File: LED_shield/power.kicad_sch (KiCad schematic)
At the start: 70 parts, among them J301 Screw_Terminal_01x02, Q301 NMOS, Q302 NMOS, Q303 NMOS, Q304 NMOS, Q305 NMOS, U301 LM25149RGYR, U302 LM25149RGYR, U303 LM74700

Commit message: Finish most of PCB design
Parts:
- removed R310, R311: 5m, Resistor_SMD:R_2010_5025Metric, symbol Device:R_US
- added NT301: NetTie_2, NetTie:NetTie-2_SMD_Pad2.0mm, symbol Device:NetTie_2
- C310: renamed from C303; LCSC (none) -> C15195
- C311: renamed from C318; LCSC (none) -> C15195
- C314: renamed from C304; LCSC (none) -> C15195
- C315: renamed from C319; LCSC (none) -> C15195
- C318: renamed from C305; LCSC (none) -> C15195
- C319: renamed from C320; LCSC (none) -> C15195
- C320: renamed from C306; LCSC (none) -> C15195
- C321: LCSC (none) -> C15195
- C322: renamed from C333; LCSC (none) -> C15195
- C323: renamed from C334; LCSC (none) -> C15195
- renumbered C335 to C301, C337 to C302, C336 to C303, C309 to C304, C301 to C305, C316 to C306, C324 to C307, C302 to C308, C317 to C309, C315 to C312, C330 to C313, C314 to C316, C329 to C317, C307 to C324, C322 to C325, C308 to C326, C323 to C327, C310 to C328, C325 to C329, C311 to C330, C326 to C331, C312 to C332, C327 to C333, C313 to C334, C328 to C335, C331 to C336, C332 to C337, R318 to R301, R305 to R302, R306 to R303, R316 to R304, R317 to R305, R307 to R306, R319 to R307, R303 to R308, R314 to R309, R308 to R310, R320 to R311, R309 to R313, R321 to R314, R323 to R315, R324 to R316, R313 to R317, R322 to R318, R304 to R319, R315 to R320, U303 to U301, U301 to U302, U302 to U303
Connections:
- net +5V: now also NT301.2
- net +5V_{b}: now also NT301.1
- no-connect marks 5 -> 7

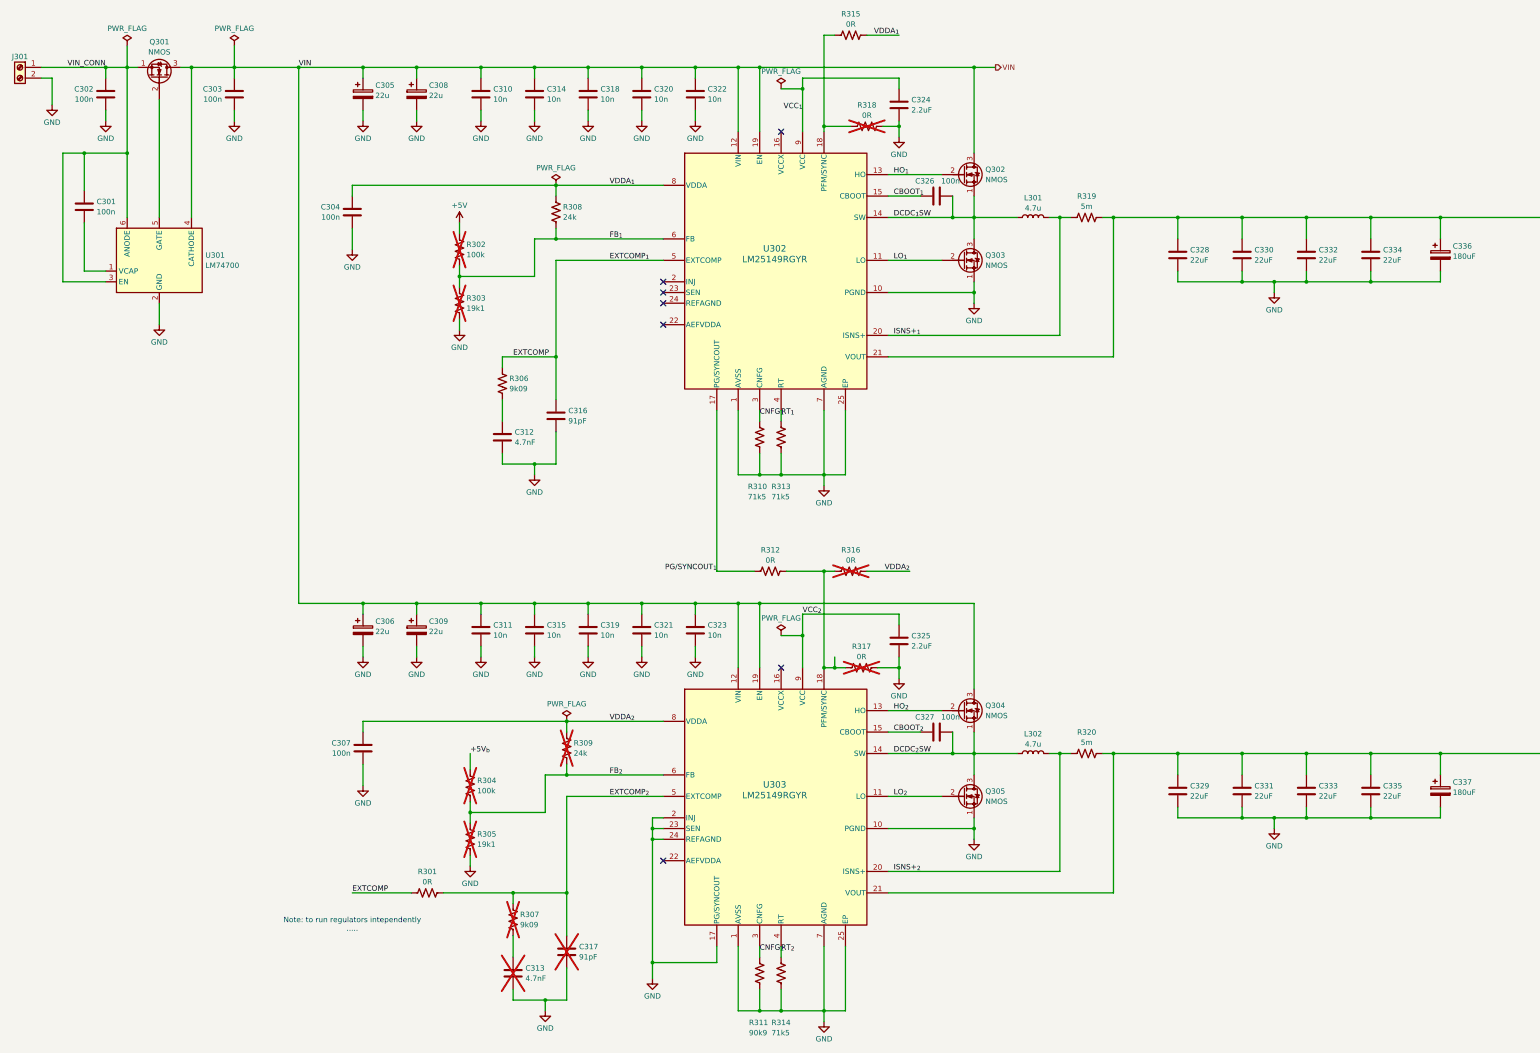
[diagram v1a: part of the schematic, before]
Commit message: Remove unused components
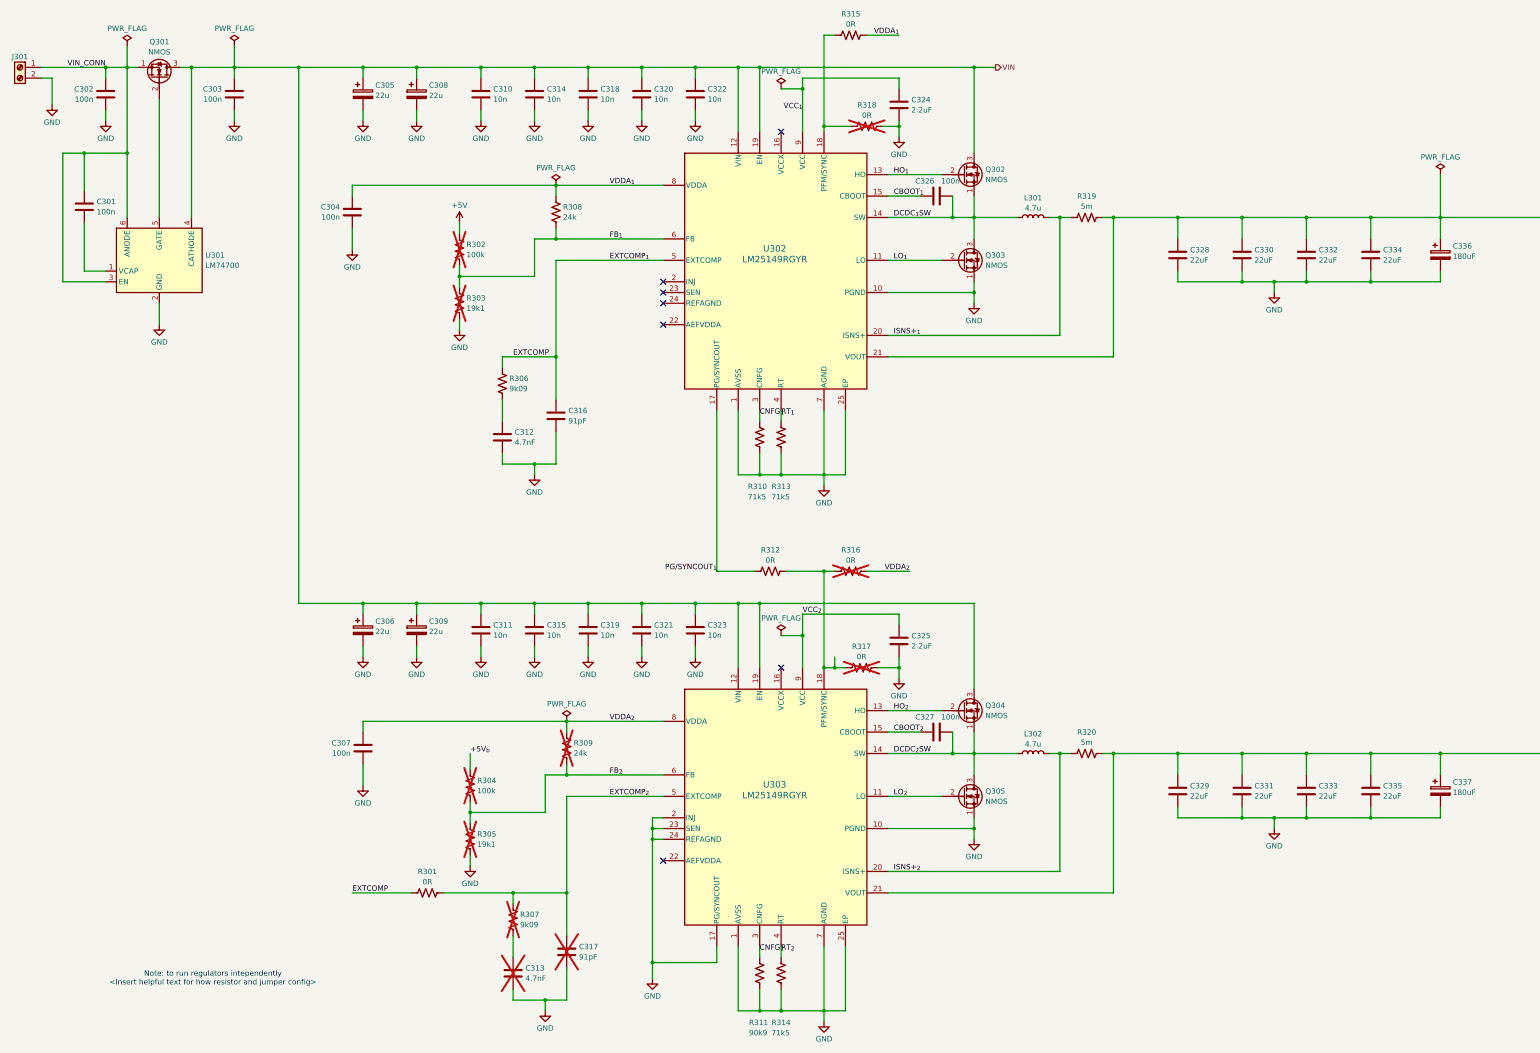
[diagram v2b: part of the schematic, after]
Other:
- note added: "Note: to run regulators intependently <Insert helpful text for how resistor and jumper config>"
- note removed: "Note: to run regulators intependently ....."
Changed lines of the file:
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@@
 	(wire
 		(pts
+			(xy 354.33 60.96) (xy 354.33 71.12)
+		)
+		(stroke
+			(width 0)
+			(type default)
+		)
+	)
+	(wire
+		(pts
 			(xy 96.52 63.5) (xy 144.78 63.5)
 		)
@@
 		)
 	)
-	(text "Note: to run regulators intependently\n....."
+	(text "Note: to run regulators intependently\n<Insert helpful text for how resistor and jumper config>"
 		(exclude_from_sim no)
-		(at 96.52 238.76 0)
+		(at 63.5 251.46 0)
 		(effects
 			(font
@@
 		)
 	)
-	(label "VIN"
-		(at 83.82 35.56 0)
-		(fields_autoplaced yes)
-		(effects
-			(font
-				(size 1.27 1.27)
-			)
-			(justify left bottom)
-		)
-	)
 	(label "HO_{1}"
 		(at 224.79 60.96 0)
@@
 					(unit 1)
 				)
+			)
+		)
+	)
+	(symbol
+		(lib_id "power:PWR_FLAG")
+		(at 354.33 60.96 0)
+		(unit 1)
+		(exclude_from_sim no)
+		(in_bom yes)
+		(on_board yes)
+		(dnp no)
+		(fields_autoplaced yes)
+		(property "Reference" "#FLG0307"
+			(at 354.33 59.055 0)
+			(effects
+				(font
+					(size 1.27 1.27)
+				)
+				(hide yes)
+			)
+		)
+		(property "Value" "PWR_FLAG"
+			(at 354.33 56.8269 0)
+			(effects
+				(font
+					(size 1.27 1.27)
+				)
+			)
+		)
+		(property "Footprint" ""
+			(at 354.33 60.96 0)
+			(effects
+				(font
+					(size 1.27 1.27)
+				)
+				(hide yes)
+			)
+		)
+		(property "Datasheet" "~"
+			(at 354.33 60.96 0)
+			(effects
+				(font
+					(size 1.27 1.27)
+				)
+				(hide yes)
+			)
+		)
+		(property "Description" "Special symbol for telling ERC where power comes from"
+			(at 354.33 60.96 0)
+			(effects
+				(font
+					(size 1.27 1.27)
+				)
+				(hide yes)
+			)
+		)
+		(pin "1"
+		)
+		(instances
+			(project "LED_shield"
+				(path "/1ea5d53d-438b-4931-b69a-e3b85be65776/e840c4ed-09f9-4c51-97a0-e8f2864c789b"
+					(reference "#FLG0307")
+					(unit 1)
+				)

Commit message: Small fixes before production
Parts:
- added R321: 82k, Resistor_SMD:R_0603_1608Metric, symbol Device:R_US
- C312, C313: value 4.7nF -> 5.6nF; LCSC (none) -> C77067
- C316, C317: value 91pF -> 470pF; LCSC (none) -> C1620
- R302, R304: footprint Resistor_SMD:R_0603_1608Metric -> Resistor_SMD:R_0402_1005Metric; LCSC (none) -> C25741
- R303, R305: LCSC (none) -> C22897
- R306, R307: value 9k09 -> 5k1; LCSC (none) -> C23186
- R310: value 71k5 -> 560k
- R311: value 90k9 -> 91k; LCSC (none) -> C23265
- R313, R314: value 71k5 -> 75k; LCSC (none) -> C23242
- U301: LCSC (none) -> C2941042
- U302, U303: LCSC (none) -> C3188827
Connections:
- net CNFG_{1}: now also R321.1
- net GND: now also R321.2
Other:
- moved on the sheet: R310, R313

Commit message: Small schematic change
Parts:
- R319, R320: footprint Resistor_SMD:R_2010_5025Metric -> Resistor_SMD:R_1206_3216Metric; LCSC C6605055 -> C5121708
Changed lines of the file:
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@@
 			)
 		)
-		(property "Footprint" "Resistor_SMD:R_2010_5025Metric"
+		(property "Footprint" "Resistor_SMD:R_1206_3216Metric"
 			(at 270.764 197.104 90)
 			(effects
@@
 			)
 		)
-		(property "LCSC" "C6605055"
+		(property "LCSC" "C5121708"
 			(at 270.51 198.12 0)
 			(effects
@@
 			)
 		)
-		(property "Footprint" "Resistor_SMD:R_2010_5025Metric"
+		(property "Footprint" "Resistor_SMD:R_1206_3216Metric"
 			(at 270.764 70.104 90)
 			(effects
@@
 			)
 		)
-		(property "LCSC" "C6605055"
+		(property "LCSC" "C5121708"
 			(at 270.51 71.12 0)
 			(effects

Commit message: Make PCB ready for manufacture (again)
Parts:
- removed C304, C307, C326, C327: 100n, Capacitor_SMD:C_0402_1005Metric, symbol Device:C
- removed C305, C306, C308, C309: 22u, Capacitor_SMD:C_Elec_6.3x5.8, symbol Device:C_Polarized
- removed C310, C311, C314, C315, C318, C319, C320, C321, C322, C323: 10n, Capacitor_SMD:C_0402_1005Metric, symbol Device:C
- removed C312, C313: 5.6nF, Capacitor_SMD:C_0603_1608Metric, symbol Device:C
- removed C316, C317: 470pF, Capacitor_SMD:C_0603_1608Metric, symbol Device:C
- removed C324, C325: 2.2uF, Capacitor_SMD:C_0603_1608Metric, symbol Device:C
- removed C328, C329, C330, C331, C332, C333, C334, C335: 22uF, Capacitor_SMD:C_0805_2012Metric, symbol Device:C
- removed C336, C337: 180uF, Capacitor_SMD:C_Elec_6.3x5.8, symbol Device:C_Polarized
- removed L301, L302: 4.7u, Inductor_SMD:L_Vishay_IHLP-6767, symbol Device:L
- removed NT301: NetTie_2, NetTie:NetTie-2_SMD_Pad2.0mm, symbol Device:NetTie_2
- removed Q302, Q303, Q304, Q305: NMOS, Package_SON:VSONP-8-1EP_5x6_P1.27mm, symbol Device:Q_NMOS_SGD
- removed R301, R312, R315, R316, R317, R318: 0R, Resistor_SMD:R_0402_1005Metric, symbol Device:R_US
- removed R302, R304: 100k, Resistor_SMD:R_0402_1005Metric, symbol Device:R_US
- removed R303, R305: 19k1, Resistor_SMD:R_0603_1608Metric, symbol Device:R_US
- removed R306, R307: 5k1, Resistor_SMD:R_0603_1608Metric, symbol Device:R_US
- removed R308, R309: 24k, Resistor_SMD:R_0603_1608Metric, symbol Device:R_US
- removed R310: 560k, Resistor_SMD:R_0603_1608Metric, symbol Device:R_US
- removed R311: 91k, Resistor_SMD:R_0603_1608Metric, symbol Device:R_US
- removed R313, R314: 75k, Resistor_SMD:R_0603_1608Metric, symbol Device:R_US
- removed R319, R320: 5m, Resistor_SMD:R_1206_3216Metric, symbol Device:R_US
- removed R321: 82k, Resistor_SMD:R_0603_1608Metric, symbol Device:R_US
- removed U302, U303: LM25149RGYR, Skrooter_footprints:RGY0024E-MFG, symbol SkrooterLib:LM25149RGYR
- added D1: BZT52-C16S-AU, Diode_SMD:D_SOD-323F, symbol Diode:BZT52Bxx
- added J1, J2, J3, J4, J5, J6: Screw_Terminal_01x02, Connector_Phoenix_MC:PhoenixContact_MCV_1,5_2-G-3.81_1x02_P3.81mm_Vertical, symbol Connector:Screw_Terminal_01x02
- added Q1: MMBT5551L, Package_TO_SOT_SMD:SOT-23, symbol Transistor_BJT:MMBT5551L
- added R1, R2: 100k, Resistor_SMD:R_0402_1005Metric, symbol Device:R_US
- C301, C302, C303: footprint Capacitor_SMD:C_0805_2012Metric -> Capacitor_SMD:C_0603_1608Metric; LCSC C28233 -> C14663
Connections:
- net +5V: now also J2.1 (Pin_1)
- net GND: now also J1.2 (Pin_2), J2.2 (Pin_2), J3.2 (Pin_2), J4.2 (Pin_2), J5.2 (Pin_2), J6.2 (Pin_2), Q1.2 (E)
- net VIN_CONN: now also D1.1 (K), R1.1; no longer U301.3 (EN)
- new net: D1.2 (A), R2.1
- new net: Q1.1 (B), R2.2
- new net DCDC0/5V_{OUT}: J1.1 (Pin_1)
- new net DCDC2/5V_{OUT}: J3.1 (Pin_1)
- new net DCDC3/5V_{OUT}: J4.1 (Pin_1)
- new net DCDC4/5V_{OUT}: J5.1 (Pin_1)
- new net DCDC5/5V_{OUT}: J6.1 (Pin_1)
- new net PROT_EN: Q1.3 (C), R1.2, U301.3 (EN)
- no-connect marks 7 -> 0
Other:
- added sheet DCDC0 (DCDC.kicad_sch)
- added sheet DCDC1 (DCDC.kicad_sch)
- added sheet DCDC2 (DCDC.kicad_sch)
- added sheet DCDC3 (DCDC.kicad_sch)
- added sheet DCDC4 (DCDC.kicad_sch)
- added sheet DCDC5 (DCDC.kicad_sch)
- note added: "5V for PICO"
- note added: "DCDCs"
- note added: "Overvoltage detection"
- note added: "Reverse polarity protection"
- note added: "Terminals for driving panels"
- note removed: "Note: to run regulators intependently <Insert helpful text for how resistor and jumper config>"
- moved on the sheet: C301, C302, C303, J301, Q301, U301
